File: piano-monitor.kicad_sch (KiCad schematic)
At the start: 1 part

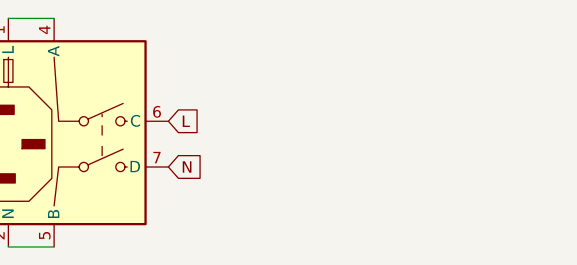
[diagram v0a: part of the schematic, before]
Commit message: Add tpa3110 footprint
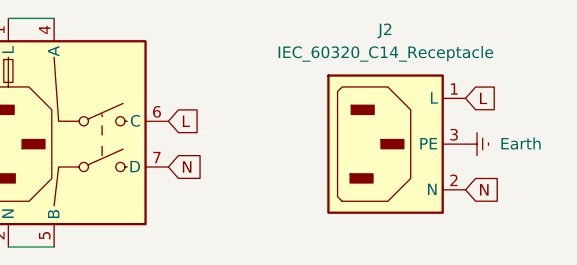
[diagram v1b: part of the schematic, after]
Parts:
- added J2: IEC_60320_C14_Receptacle, symbol Connector:IEC_60320_C14_Receptacle
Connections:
- net Earth: now also J2.3 (PE)
- net L: now also J2.1 (L)
- net N: now also J2.2 (N)
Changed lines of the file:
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@@
+		)
+	)
+	(global_label "L"
+		(shape input)
+		(at 151.13 57.15 0)
+		(fields_autoplaced yes)
+		(effects
+			(font
+				(size 1.27 1.27)
+			)
+			(justify left)
+		)
+		(property "Intersheetrefs" "${INTERSHEET_REFS}"
+			(at 155.1433 57.15 0)
+			(effects
+				(font
+					(size 1.27 1.27)
+				)
+				(justify left)
+				(hide yes)
+			)
+		)
+	)
+	(global_label "N"
+		(shape input)
+		(at 151.13 67.31 0)
+		(fields_autoplaced yes)
+		(effects
+			(font
+				(size 1.27 1.27)
+			)
+			(justify left)
+		)
+		(property "Intersheetrefs" "${INTERSHEET_REFS}"
+			(at 155.4457 67.31 0)
+			(effects
+				(font
+					(size 1.27 1.27)
+				)
+				(justify left)
+				(hide yes)
+			)
 		)
 	)
@@
 	)
 	(symbol
+		(lib_id "power:Earth")
+		(at 151.13 62.23 90)
+		(unit 1)
+		(exclude_from_sim no)
+		(in_bom yes)
+		(on_board yes)
+		(dnp no)
+		(fields_autoplaced yes)
+		(property "Reference" "#PWR02"
+			(at 157.48 62.23 0)
+			(effects
+				(font
+					(size 1.27 1.27)
+				)
+				(hide yes)
+			)
+		)
+		(property "Value" "Earth"
+			(at 154.94 62.2299 90)
+			(effects
+				(font
+					(size 1.27 1.27)
+				)
+				(justify right)
+			)
+		)
+		(property "Footprint" ""
+			(at 151.13 62.23 0)
+			(effects
+				(font
+					(size 1.27 1.27)
+				)
+				(hide yes)
+			)
+		)
+		(property "Datasheet" "~"
+			(at 151.13 62.23 0)
+			(effects
+				(font
+					(size 1.27 1.27)
+				)
+				(hide yes)
+			)
+		)
+		(property "Description" "Power symbol creates a global label with name \"Earth\""
+			(at 151.13 62.23 0)
+			(effects
+				(font
+					(size 1.27 1.27)
+				)
+				(hide yes)
+			)
+		)
+		(pin "1"
+		)
+		(instances
+			(project "piano-monitor"
+				(path "/a27efd99-174e-47e5-804a-22be857a638b"
+					(reference "#PWR02")
+					(unit 1)
+				)
+			)
+		)
+	)
+	(symbol
 		(lib_id "iec320-c14:iec320-c14")
 		(at 102.87 62.23 0)
@@
 					(unit 1)
 				)
+			)
+		)
+	)
+	(symbol
+		(lib_id "Connector:IEC_60320_C14_Receptacle")
+		(at 142.24 62.23 0)
+		(unit 1)
+		(exclude_from_sim no)
+		(in_bom yes)
+		(on_board yes)
+		(dnp no)
+		(fields_autoplaced yes)
+		(property "Reference" "J2"
+			(at 142.24 49.53 0)
+			(effects
+				(font
+					(size 1.27 1.27)
+				)
+			)
+		)
+		(property "Value" "IEC_60320_C14_Receptacle"
+			(at 142.24 52.07 0)
+			(effects
+				(font
+					(size 1.27 1.27)
+				)
+			)
+		)
+		(property "Footprint" ""
+			(at 139.954 62.23 0)
+			(effects
+				(font
+					(size 1.27 1.27)
+				)
+				(hide yes)
+			)
+		)
+		(property "Datasheet" "~"
+			(at 139.954 62.23 0)
+			(effects
+				(font
+					(size 1.27 1.27)
+				)
+				(hide yes)
+			)
+		)
+		(property "Description" "C14 Plug, 10A max"
+			(at 141.605 62.23 0)
+			(effects
+				(font
+					(size 1.27 1.27)
+				)
+				(hide yes)
+			)
+		)
+		(pin "1"
+		)
+		(pin "3"
+		)
+		(pin "2"
+		)
+		(instances
+			(project ""
+				(path "/a27efd99-174e-47e5-804a-22be857a638b"
+					(reference "J2")
+					(unit 1)
+				)

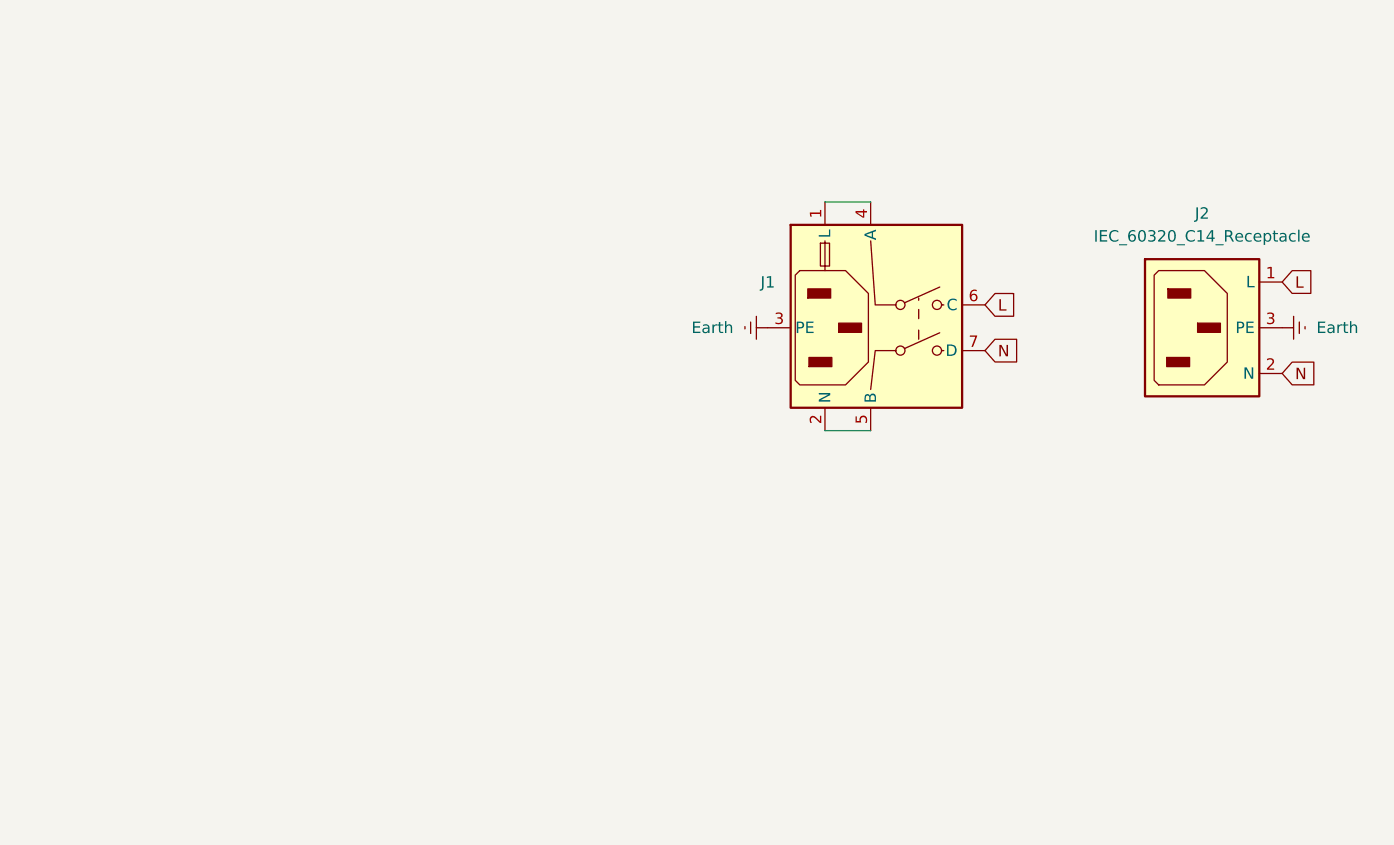
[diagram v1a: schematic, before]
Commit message: Add initial schematic
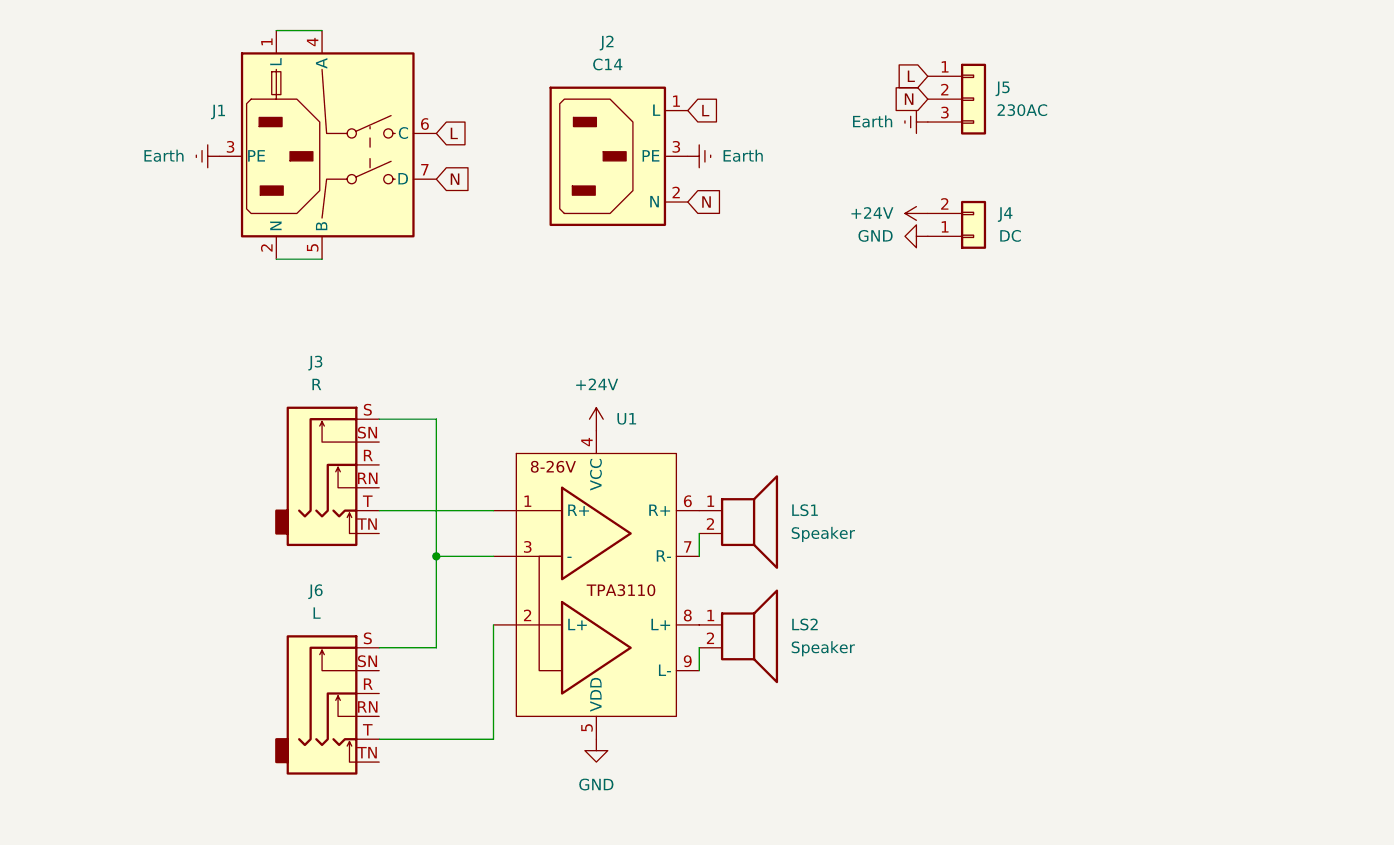
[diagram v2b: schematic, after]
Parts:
- added J3: R, symbol Connector_Audio:AudioJack3_Switch
- added J4: DC, Connector_PinHeader_2.54mm:PinHeader_1x02_P2.54mm_Vertical, symbol Connector_Generic:Conn_01x02
- added J5: 230AC, Connector_PinHeader_2.54mm:PinHeader_1x03_P2.54mm_Vertical, symbol Connector_Generic:Conn_01x03
- added J6: L, symbol Connector_Audio:AudioJack3_Switch
- added LS1, LS2: Speaker, symbol Device:Speaker
- added U1: ~, tpa3110:tpa3110, symbol tpa3110:tpa3110
- J2: value IEC_60320_C14_Receptacle -> C14
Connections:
- net Earth: now also J5.3 (Pin_3)
- net L: now also J5.1 (Pin_1)
- net N: now also J5.2 (Pin_2)
- new net: LS1.1, U1.6 (R+)
- new net: LS1.2, U1.7 (R-)
- new net: J3.S, J6.S, U1.3 (-)
- new net: J3.T, U1.1 (R+)
- new net: LS2.1, U1.8 (L+)
- new net: LS2.2, U1.9 (L-)
- new net: J6.T, U1.2 (L+)
- new net +24V: J4.2 (Pin_2), U1.4 (VCC)
- new net GND: J4.1 (Pin_1), U1.5 (VDD)
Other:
- moved on the sheet: J1, J2

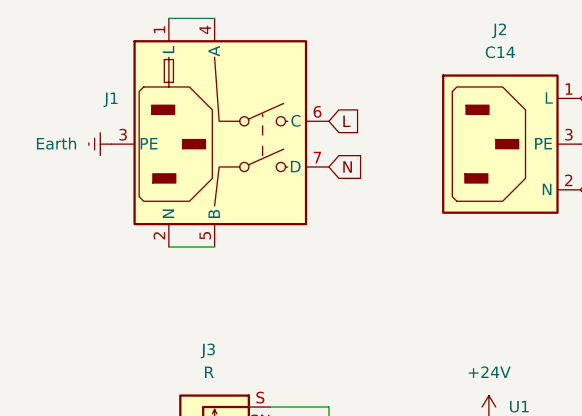
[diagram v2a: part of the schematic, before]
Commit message: Update the C14 plug symbol and footprint
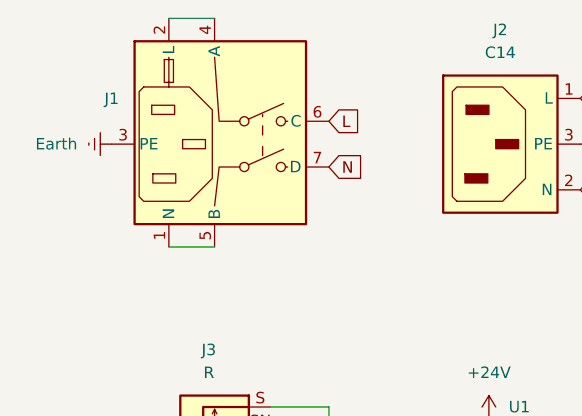
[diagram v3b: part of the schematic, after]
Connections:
- net at J1.1 (N): now also J1.5 (B); no longer J1.4 (A)
- net at J1.2 (L): now also J1.4 (A); no longer J1.5 (B)

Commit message: Update Schematic
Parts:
- removed J2: C14, symbol Connector:IEC_60320_C14_Receptacle
- removed J3: R, symbol Connector_Audio:AudioJack3_Switch
- removed J6: L, symbol Connector_Audio:AudioJack3_Switch
- added J3, J7: NCJ6FA-V, Connector_Audio:Jack_XLR-6.35mm_Neutrik_NCJ6FA-V_Vertical, symbol Connector_Audio:NCJ6FA-V
- added J6: ~, c14-outlet:c14-outlet, symbol c14-outlet:c14-outlet
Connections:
- net Earth: now also J6.3 (PE)
- net GND: no longer U1.5 (VDD)
- net L: now also J6.1 (L)
- net N: now also J6.2 (N)
- net GNDA: now reaches U1.3 (-)
- net GNDA: now also U1.5 (VDD), J3.1, J3.G, J3.S, J7.1, J7.G, J7.S
- net T1: now reaches U1.1 (R+)
- net T1: now also J7.2, J7.T
- net T2: now reaches U1.2 (L+)
- net T2: now also J3.2, J3.T
- new net R1: J7.3, J7.R
- new net R2: J3.3, J3.R

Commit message: Add some traces
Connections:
- net R1: no longer names the net of J7.R
- net R1: no longer J7.3
- net R2: no longer names the net of J3.3
- net R2: no longer J3.R
- no-connect marks 0 -> 4
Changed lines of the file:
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@@
 		(color 0 0 0 0)
 	)
+	(no_connect
+		(at 50.8 80.01)
+	)
+	(no_connect
+		(at 50.8 105.41)
+	)
+	(no_connect
+		(at 24.13 111.76)
+	)
+	(no_connect
+		(at 24.13 86.36)
+	)
 	(wire
 		(pts
@@
 		)
 	)
-	(global_label "R1"
-		(shape input)
-		(at 50.8 80.01 0)
+	(global_label "S2"
+		(shape input)
+		(at 53.34 102.87 90)
 		(fields_autoplaced yes)
 		(effects
@@
 		)
 		(property "Intersheetrefs" "${INTERSHEET_REFS}"
-			(at 56.2647 80.01 0)
+			(at 53.34 97.4658 90)
 			(effects
 				(font
@@
 		)
 	)
-	(global_label "R2"
-		(shape input)
-		(at 50.8 105.41 0)
-		(fields_autoplaced yes)
-		(effects
-			(font
-				(size 1.27 1.27)
-			)
-			(justify left)
-		)
-		(property "Intersheetrefs" "${INTERSHEET_REFS}"
-			(at 56.2647 105.41 0)
-			(effects
-				(font
-					(size 1.27 1.27)
-				)
-				(justify left)
+	(global_label "T1"
+		(shape input)
+		(at 53.34 82.55 270)
+		(fields_autoplaced yes)
+		(effects
+			(font
+				(size 1.27 1.27)
+			)
+			(justify right)
+		)
+		(property "Intersheetrefs" "${INTERSHEET_REFS}"
+			(at 53.34 87.7123 90)
+			(effects
+				(font
+					(size 1.27 1.27)
+				)
+				(justify right)
+				(hide yes)
+			)
+		)
+	)
+	(global_label "N"
+		(shape input)
+		(at 111.76 36.83 180)
+		(fields_autoplaced yes)
+		(effects
+			(font
+				(size 1.27 1.27)
+			)
+			(justify right)
+		)
+		(property "Intersheetrefs" "${INTERSHEET_REFS}"
+			(at 107.4443 36.83 0)
+			(effects
+				(font
+					(size 1.27 1.27)
+				)
+				(justify right)
 				(hide yes)
 			)
@@
 	(global_label "S2"
 		(shape input)
-		(at 53.34 102.87 90)
-		(fields_autoplaced yes)
-		(effects
-			(font
-				(size 1.27 1.27)
-			)
-			(justify left)
-		)
-		(property "Intersheetrefs" "${INTERSHEET_REFS}"
-			(at 53.34 97.4658 90)
-			(effects
-				(font
-					(size 1.27 1.27)
-				)
-				(justify left)
-				(hide yes)
-			)
-		)
-	)
-	(global_label "T1"
-		(shape input)
-		(at 53.34 82.55 270)
-		(fields_autoplaced yes)
-		(effects
-			(font
-				(size 1.27 1.27)
-			)
-			(justify right)
-		)
-		(property "Intersheetrefs" "${INTERSHEET_REFS}"
-			(at 53.34 87.7123 90)
-			(effects
-				(font
-					(size 1.27 1.27)
-				)
-				(justify right)
-				(hide yes)
-			)
-		)
-	)
-	(global_label "N"
-		(shape input)
-		(at 111.76 36.83 180)
-		(fields_autoplaced yes)
-		(effects
-			(font
-				(size 1.27 1.27)
-			)
-			(justify right)
-		)
-		(property "Intersheetrefs" "${INTERSHEET_REFS}"
-			(at 107.4443 36.83 0)
-			(effects
-				(font
-					(size 1.27 1.27)
-				)
-				(justify right)
-				(hide yes)
-			)
-		)
-	)
-	(global_label "R1"
-		(shape input)
-		(at 24.13 86.36 270)
-		(fields_autoplaced yes)
-		(effects
-			(font
-				(size 1.27 1.27)
-			)
-			(justify right)
-		)
-		(property "Intersheetrefs" "${INTERSHEET_REFS}"
-			(at 24.13 91.8247 90)
-			(effects
-				(font
-					(size 1.27 1.27)
-				)
-				(justify right)
-				(hide yes)
-			)
-		)
-	)
-	(global_label "S2"
-		(shape input)
 		(at 16.51 104.14 180)
 		(fields_autoplaced yes)
@@
 			(effects
 				(font
-					(size 1.27 1.27)
-				)
-				(justify right)
-				(hide yes)
-			)
-		)
-	)
-	(global_label "R2"
-		(shape input)
-		(at 24.13 111.76 270)
-		(fields_autoplaced yes)
-		(effects
-			(font
-				(size 1.27 1.27)
-			)
-			(justify right)
-		)
-		(property "Intersheetrefs" "${INTERSHEET_REFS}"
-			(at 24.13 117.2247 90)
-			(effects
-				(font

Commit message: Update schematic and prepare for the AC pcb to be milled out with a 0.8mm bit
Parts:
- removed J5: 230AC, Connector_PinHeader_2.54mm:PinHeader_1x03_P2.54mm_Vertical, symbol Connector_Generic:Conn_01x03
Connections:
- net N_PRESWITCH: now reaches J1.1 (N), J1.5 (B)
- net L_PRESWITCH: now reaches J1.2 (L), J1.4 (A)
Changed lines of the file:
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@@
+	(wire
+		(pts
+			(xy 29.21 43.18) (xy 33.02 43.18)
+		)
+		(stroke
+			(width 0)
+			(type default)
+		)
+	)
 	(wire
 		(pts
@@
 		)
 	)
+	(global_label "EARTH"
+		(shape input)
+		(at 30.48 43.18 270)
+		(fields_autoplaced yes)
+		(effects
+			(font
+				(size 1.27 1.27)
+			)
+			(justify right)
+		)
+		(property "Intersheetrefs" "${INTERSHEET_REFS}"
+			(at 30.48 51.9709 90)
+			(effects
+				(font
+					(size 1.27 1.27)
+				)
+				(justify right)
+				(hide yes)
+			)
+		)
+	)
 	(global_label "T1"
 		(shape input)
@@
 		)
 	)
+	(global_label "N_PRESWITCH"
+		(shape input)
+		(at 39.37 54.61 180)
+		(fields_autoplaced yes)
+		(effects
+			(font
+				(size 1.27 1.27)
+			)
+			(justify right)
+		)
+		(property "Intersheetrefs" "${INTERSHEET_REFS}"
+			(at 23.5639 54.61 0)
+			(effects
+				(font
+					(size 1.27 1.27)
+				)
+				(justify right)
+				(hide yes)
+			)
+		)
+	)
 	(global_label "S2"
 		(shape input)
@@
 		)
 	)
-	(global_label "N"
+	(global_label "L_PRESWITCH"
 		(shape input)
-		(at 111.76 36.83 180)
+		(at 39.37 29.21 180)
 		(fields_autoplaced yes)
 		(effects
@@
 		)
 		(property "Intersheetrefs" "${INTERSHEET_REFS}"
-			(at 107.4443 36.83 0)
+			(at 23.8663 29.21 0)
 			(effects
 				(font
@@
 		)
 	)
-	(global_label "L"
+	(global_label "S1"
 		(shape input)
-		(at 111.76 34.29 180)
+		(at 53.34 77.47 90)
 		(fields_autoplaced yes)
 		(effects
@@
 				(size 1.27 1.27)
 			)
-			(justify right)
-		)
-		(property "Intersheetrefs" "${INTERSHEET_REFS}"
-			(at 107.7467 34.29 0)
-			(effects
-				(font
-					(size 1.27 1.27)
-				)
-				(justify right)
-				(hide yes)
-			)
-		)
-	)
-	(global_label "S1"
-		(shape input)
-		(at 53.34 77.47 90)
-		(fields_autoplaced yes)
-		(effects
-			(font
-				(size 1.27 1.27)
-			)
 			(justify left)
 		)
@@
 	(symbol
 		(lib_id "power:Earth")
-		(at 33.02 43.18 270)
+		(at 29.21 43.18 270)
 		(unit 1)
 		(exclude_from_sim no)
@@
 		(fields_autoplaced yes)
 		(property "Reference" "#PWR01"
-			(at 26.67 43.18 0)
+			(at 22.86 43.18 0)
 			(effects
 				(font
@@
 		)
 		(property "Value" "Earth"
-			(at 29.21 43.1799 90)
+			(at 25.4 43.1799 90)
 			(effects
 				(font
@@
 		)
 		(property "Footprint" ""
-			(at 33.02 43.18 0)
+			(at 29.21 43.18 0)
 			(effects
 				(font
@@
 		)
 		(property "Datasheet" "~"
-			(at 33.02 43.18 0)
+			(at 29.21 43.18 0)
 			(effects
 				(font
@@
 		)
 		(property "Description" "Power symbol creates a global label with name \"Earth\""
-			(at 33.02 43.18 0)
+			(at 29.21 43.18 0)
 			(effects
 				(font
@@
 	)
 	(symbol
-		(lib_id "power:Earth")
-		(at 111.76 39.37 270)
-		(unit 1)
-		(exclude_from_sim no)
-		(in_bom yes)
-		(on_board yes)
-		(dnp no)
-		(fields_autoplaced yes)
-		(property "Reference" "#PWR05"
-			(at 105.41 39.37 0)
-			(effects
-				(font
-					(size 1.27 1.27)
-				)
-				(hide yes)
-			)
-		)
-		(property "Value" "Earth"
-			(at 107.95 39.3699 90)
-			(effects
-				(font
-					(size 1.27 1.27)
-				)
-				(justify right)
-			)
-		)
-		(property "Footprint" ""
-			(at 111.76 39.37 0)
-			(effects
-				(font
-					(size 1.27 1.27)
-				)
-				(hide yes)
-			)
-		)
-		(property "Datasheet" "~"
-			(at 111.76 39.37 0)
-			(effects
-				(font
-					(size 1.27 1.27)
-				)
-				(hide yes)
-			)
-		)
-		(property "Description" "Power symbol creates a global label with name \"Earth\""
-			(at 111.76 39.37 0)
-			(effects
-				(font
-					(size 1.27 1.27)
-				)
-				(hide yes)
-			)
-		)
-		(pin "1"
-		)
-		(instances
-			(project "piano-monitor"
-				(path "/a27efd99-174e-47e5-804a-22be857a638b"
-					(reference "#PWR05")
-					(unit 1)
-				)
-			)
-		)
-	)
-	(symbol
 		(lib_id "Connector_Audio:NCJ6FA-V")
 		(at 45.72 105.41 0)
@@
 				)
 			)
-		)
-	)
-	(symbol
-		(lib_id "Connector_Generic:Conn_01x03")
-		(at 116.84 36.83 0)
-		(unit 1)
-		(exclude_from_sim no)
-		(in_bom yes)
-		(on_board yes)
-		(dnp no)
-		(fields_autoplaced yes)
-		(property "Reference" "J5"
-			(at 119.38 35.5599 0)
-			(effects
-				(font
-					(size 1.27 1.27)
-				)
-				(justify left)
-			)
-		)
-		(property "Value" "230AC"
-			(at 119.38 38.0999 0)
-			(effects
-				(font
-					(size 1.27 1.27)
-				)
-				(justify left)
-			)
-		)
-		(property "Footprint" "Connector_PinHeader_2.54mm:PinHeader_1x03_P2.54mm_Vertical"
-			(at 116.84 36.83 0)
-			(effects
-				(font
-					(size 1.27 1.27)
-				)
-				(hide yes)
-			)
-		)
-		(property "Datasheet" "~"
-			(at 116.84 36.83 0)
-			(effects
-				(font
-					(size 1.27 1.27)
-				)
-				(hide yes)
-			)
-		)
-		(property "Description" "Generic connector, single row, 01x03, script generated (kicad-library-utils/schlib/autogen/connector/)"
-			(at 116.84 36.83 0)
-			(effects
-				(font
-					(size 1.27 1.27)
-				)
-				(hide yes)
-			)
-		)
-		(pin "2"
-		)
-		(pin "3"
-		)
-		(pin "1"
-		)
-		(instances
-			(project ""
-				(path "/a27efd99-174e-47e5-804a-22be857a638b"
-					(reference "J5")
-					(unit 1)
-				)
-			)

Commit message: Finalise the AMP pcb
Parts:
- added J2: Conn_01x03, Connector_PinHeader_2.54mm:PinHeader_1x03_P2.54mm_Vertical, symbol Connector_Generic:Conn_01x03
- LS1, LS2: footprint (none) -> Connector_PinHeader_2.54mm:PinHeader_1x02_P2.54mm_Vertical
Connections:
- net GNDA is gone; now on net GND: J3.1, J3.G, J3.S, J7.1, J7.G, J7.S, U1.3 (-), U1.5 (VDD)
- net GND: now also J2.1 (Pin_1)
- net T1 renamed Right
- net Right: now also J2.2 (Pin_2)
- net T2 renamed Left
- net Left: now also J2.3 (Pin_3)
